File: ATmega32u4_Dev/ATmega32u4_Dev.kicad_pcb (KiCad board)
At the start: 4 copper layers, 25.5 x 40.7 mm, 34 parts, among them J1 USB4105-GF-A, J2 ICSP HEader 2x3, J3 Conn_01x14_Pin, J4 Conn_01x14_Pin, SW1 1825910-6, U1 ATmega32U4-A, U2 USBLC6-2SC6, Y1 ABM8-16.000MHZ-10-1-U-T

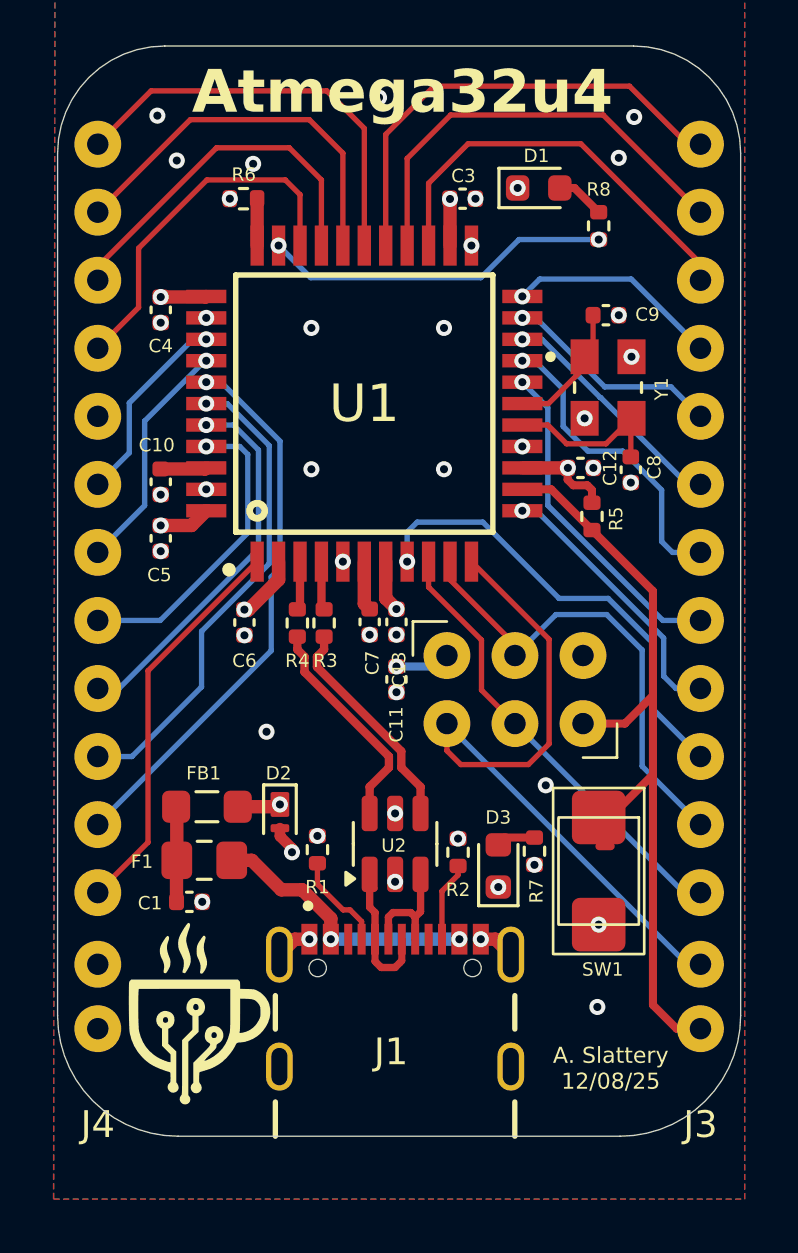
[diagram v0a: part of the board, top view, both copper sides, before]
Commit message: Cleaned up atmega and made atmega32 README
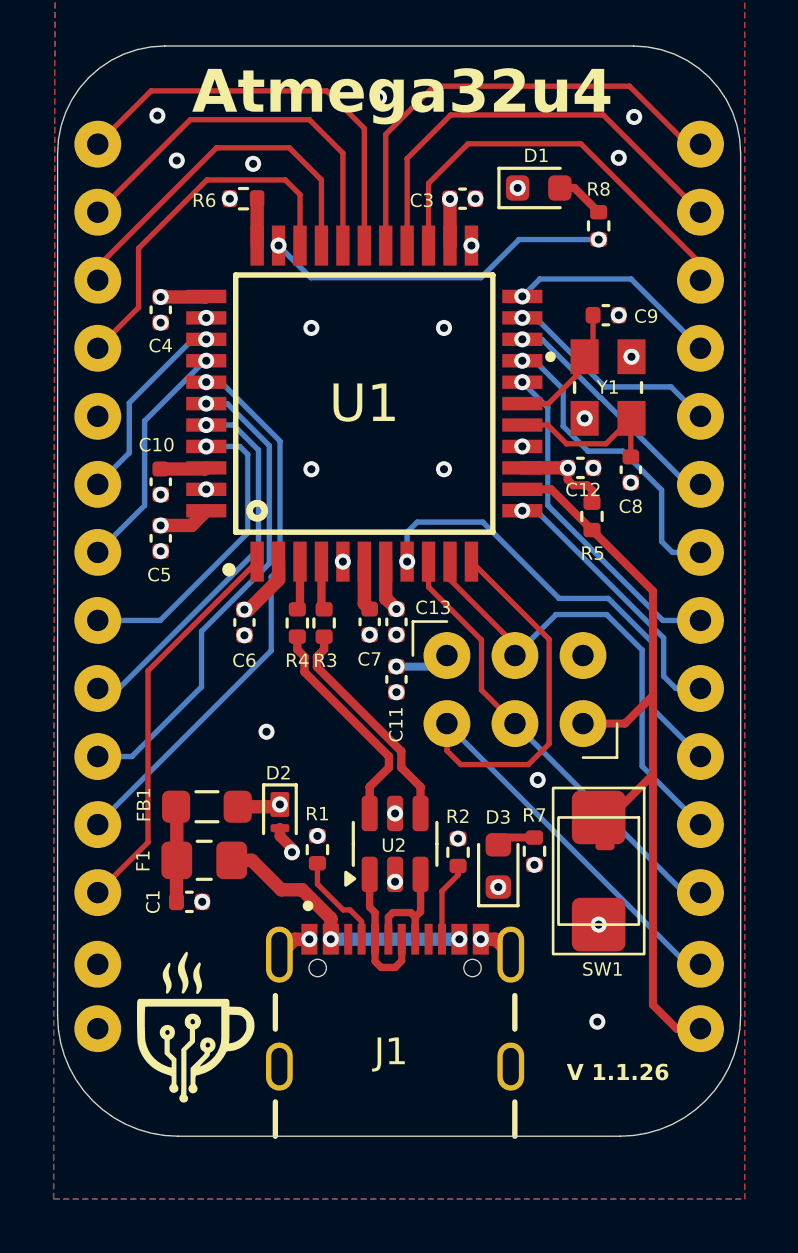
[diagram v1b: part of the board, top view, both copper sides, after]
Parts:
- moved G*** 0.57 mm to (151.4, 114.1)
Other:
- board text added: "Right Pins: 6 12 4 TXLED 1 0 2 3"
- board text added: "V 1.1.26"
- board text removed: "A. Slattery 12/08/25"

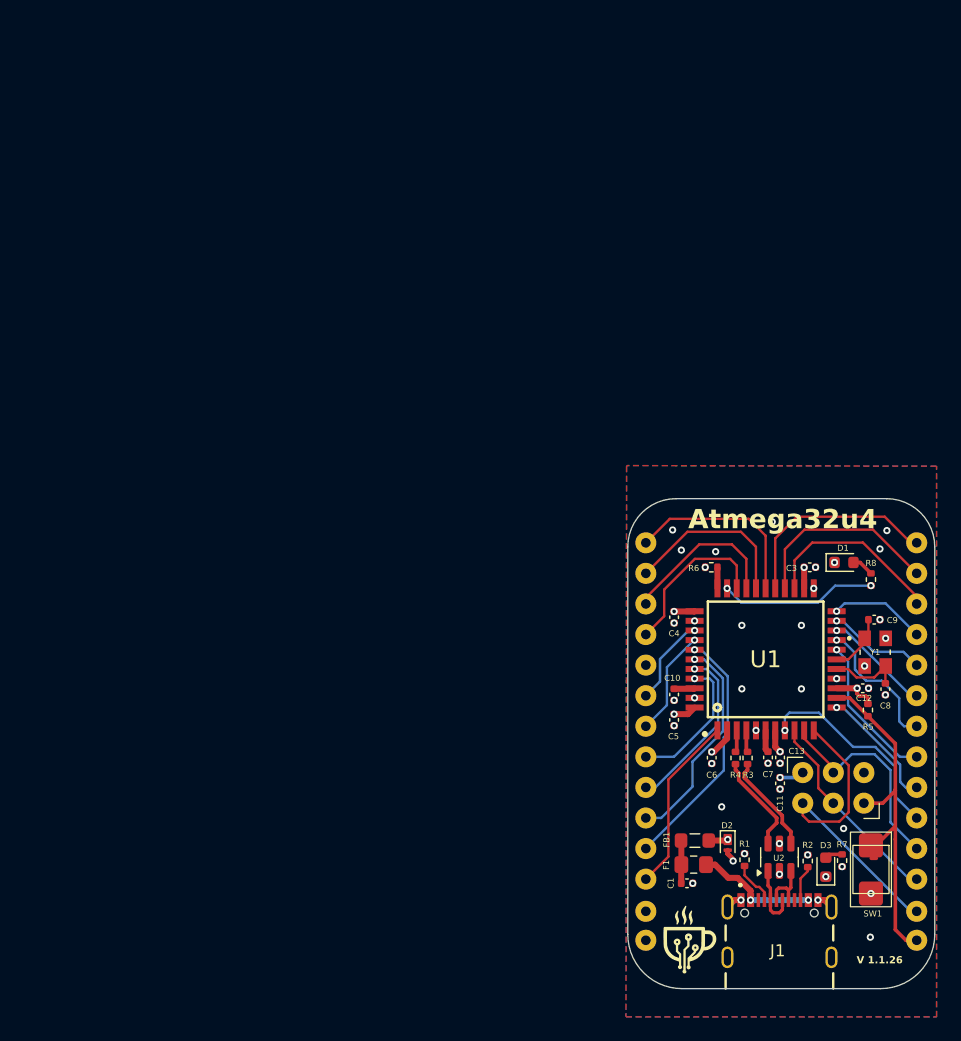
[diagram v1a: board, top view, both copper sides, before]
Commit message: Added additional board folders, updataed RP2040, ATmega, and ESP32
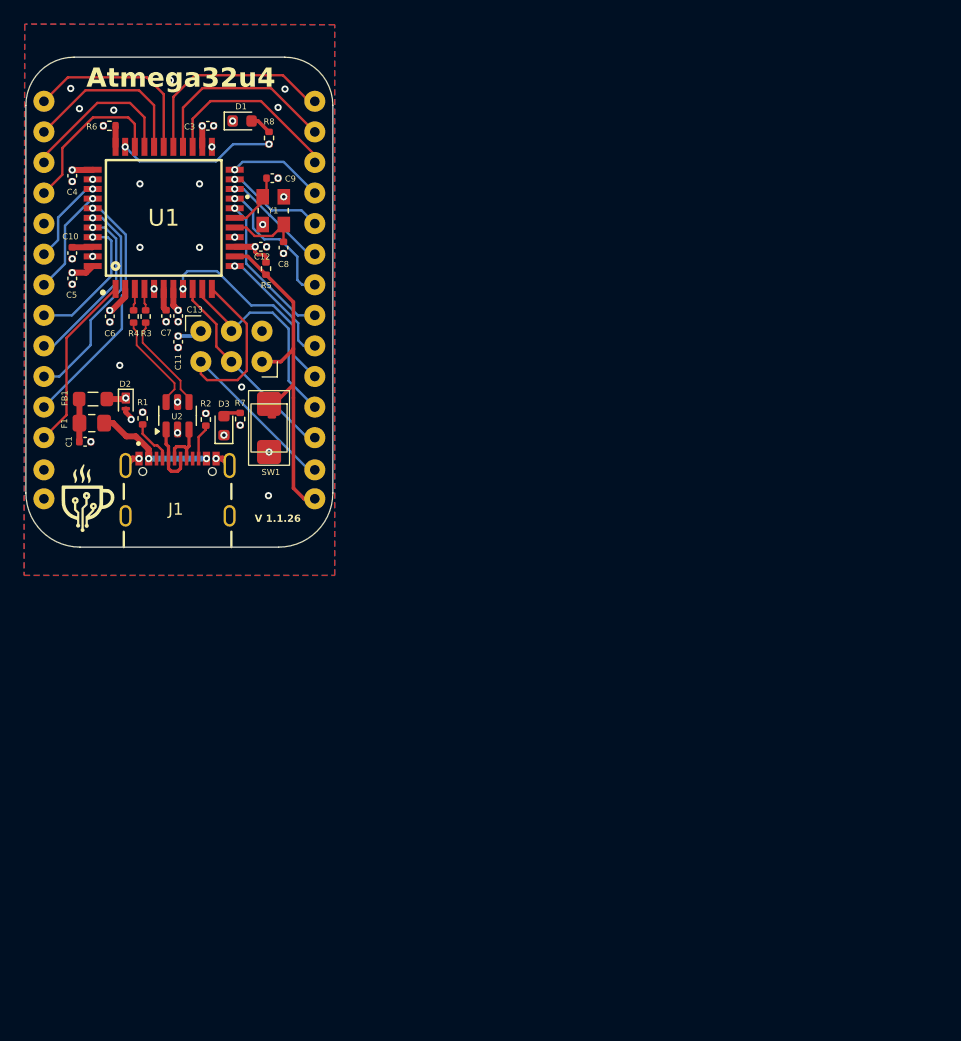
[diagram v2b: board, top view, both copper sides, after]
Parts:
- moved C12 62.0 mm to (115.8, 56.5)
- moved R7 62.0 mm to (114.1, 70.8)
- moved Y1 62.0 mm to (116.8, 53.5)
- moved D2 62.0 mm to (104.5, 69.4)
- moved C10 62.0 mm to (100.1, 57.0)
- moved C11 62.0 mm to (108.9, 64.4)
- moved C13 62.0 mm to (108.9, 62.3)
- moved C3 62.0 mm to (111.4, 46.5)
- moved C4 62.0 mm to (100.1, 50.6)
- moved C5 62.0 mm to (100.1, 59.2)
- moved C6 62.0 mm to (103.2, 62.3)
- moved C7 62.0 mm to (107.9, 62.3)
- moved C8 62.0 mm to (117.7, 56.6)
- moved C9 62.0 mm to (116.7, 50.8)
- moved D1 62.0 mm to (114.2, 46.1)
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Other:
- board text removed: "Right Pins: 6 12 4 TXLED 1 0 2 3"
